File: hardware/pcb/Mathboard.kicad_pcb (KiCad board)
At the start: 4 copper layers, 95.6 x 73.6 mm, 91 parts, among them J3 TYPE-C sinking plate, Q1 2N7002VC-, Q2 2N7002VC-, SW1 SW_Push, SW10 SW_Push, SW11 SW_Push, SW12 SW_Push, SW13 SW_Push, SW14 SW_Push, SW15 SW_Push, SW16 SW_Push, SW17 MSK13C02, SW18 SWITCH, SW2 SW_Push, SW3 SW_Push, SW4 SW_Push, SW5 SW_Push, SW6 SW_Push, SW7 SW_Push, SW8 SW_Push, SW9 SW_Push, U1 W25Q64JV, U3 USBLC6-2P6, U4 XC6206P332MR-G, U5 PSSI2021SAY, U6 RP2040, U7 74LVC1T45, Y1 12MHz

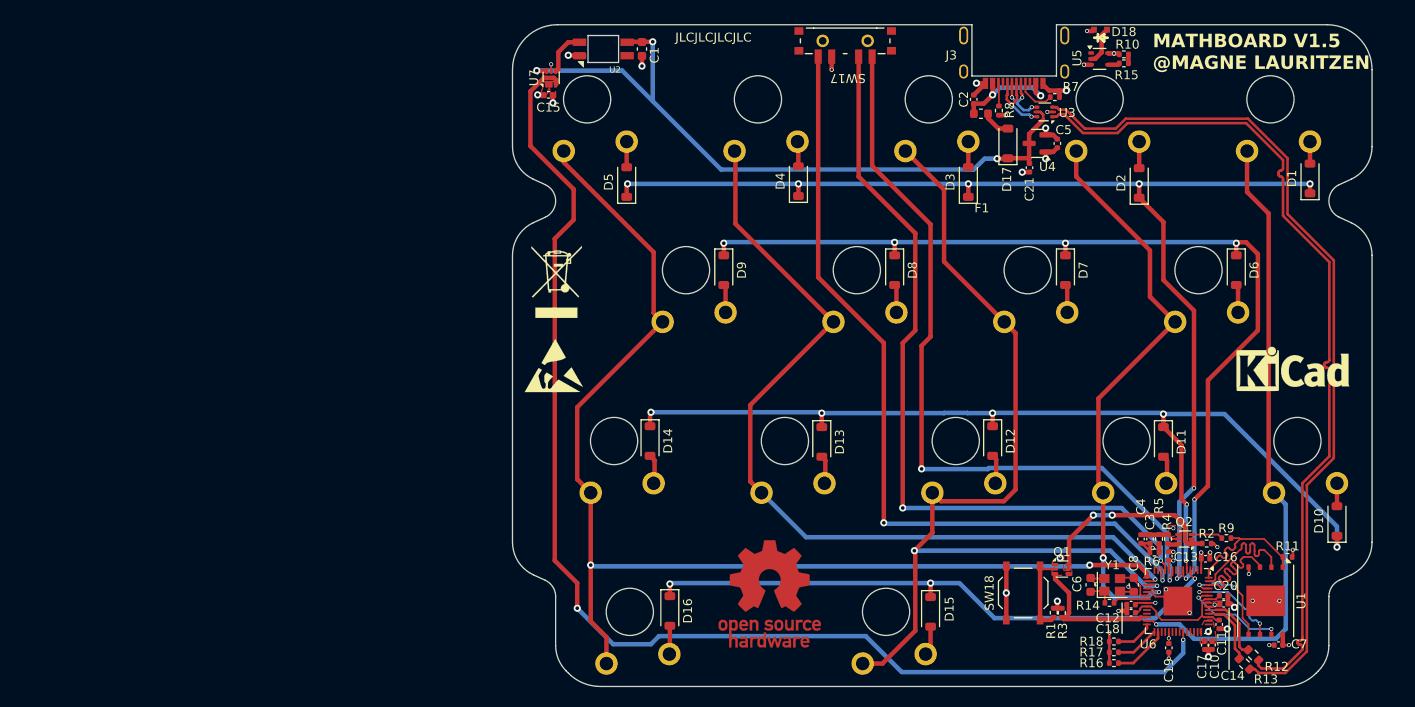
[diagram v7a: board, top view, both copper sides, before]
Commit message: V1.5
Minor changes:
Recessed the USB port
Removed ESD warning label
Moved the reset button to the center
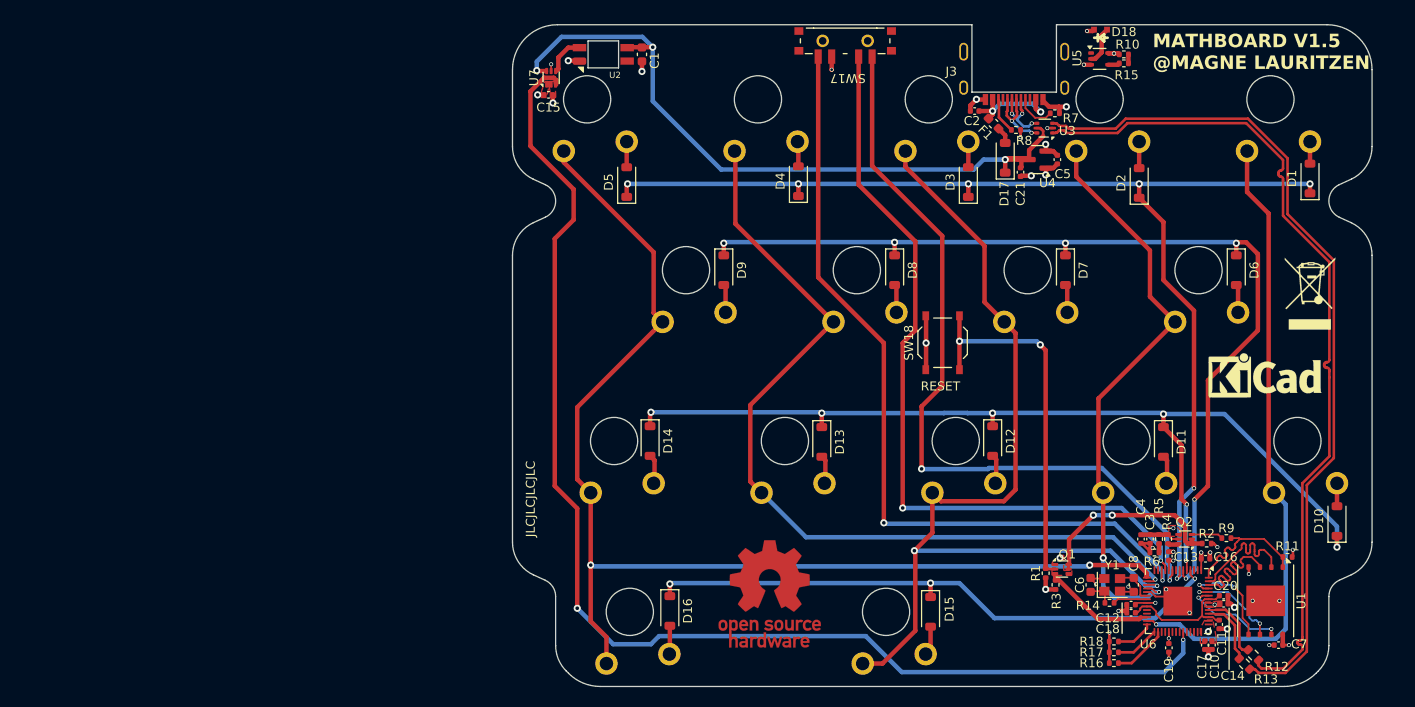
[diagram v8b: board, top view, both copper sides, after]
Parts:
- removed the REF** at (88.6, 80.6)
- moved REF** 83.8 mm to (172.7, 72.6)
- moved SW18 29.2 mm to (131.8, 78.1)
- moved R1 4.49 mm to (143.3, 103.7), turned to 90 degrees
- moved R3 3.19 mm to (144.4, 105.0), turned to 90 degrees
- moved REF** 3.19 mm to (167.7, 82.2)
- moved R8 2.87 mm to (140.0, 54.4), turned to 180 degrees
- moved C5 1.80 mm to (144.6, 57.7)
- moved U3 1.80 mm to (143.2, 54.2)
- moved U4 1.80 mm to (142.4, 57.7)
- moved J3 1.80 mm to (139.8, 47.0)
- moved R7 1.80 mm to (144.3, 52.5)
- moved F1 1.78 mm to (137.5, 53.7), turned to -45 degrees
- moved D17 1.63 mm to (138.8, 57.5)
- moved C2 1.30 mm to (135.4, 52.3), turned to 0 degrees
- moved C21 1.12 mm to (140.5, 59.1)
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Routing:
- net /Microcontroller/RESET: track 9.46 -> 41.4 mm, vias 0 -> 2
- net +5V: track 77.3 -> 80.6 mm
- net /Microcontroller/RST: track 15.6 -> 13.0 mm
- net Net-(J3-CC2): track 2.94 -> 4.37 mm
- net Net-(D17-A): track 3.18 -> 1.90 mm
- net VBUS: track 12.6 -> 11.6 mm
- net /Microcontroller/7: track 86.0 -> 87.0 mm
- net /Microcontroller/USB-: track 95.2 -> 94.4 mm
- net /Microcontroller/USB+: track 95.0 -> 94.3 mm
- net +3V3: track 17.7 -> 18.4 mm
- net /RGB_DIN: track 5.00 -> 4.40 mm
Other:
- outline, holes or cut-outs redrawn
- board text added: "RESET"
